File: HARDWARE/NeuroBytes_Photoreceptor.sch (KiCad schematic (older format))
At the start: 19 parts, among them P1 CONN_01X04, P2 CONN_01X04, P3 CONN_01X07, SW1 SW_PUSH, SW2 SW_PUSH, U1 APDS9007, U2 STM32L011Gx, U3 LD3985M33R

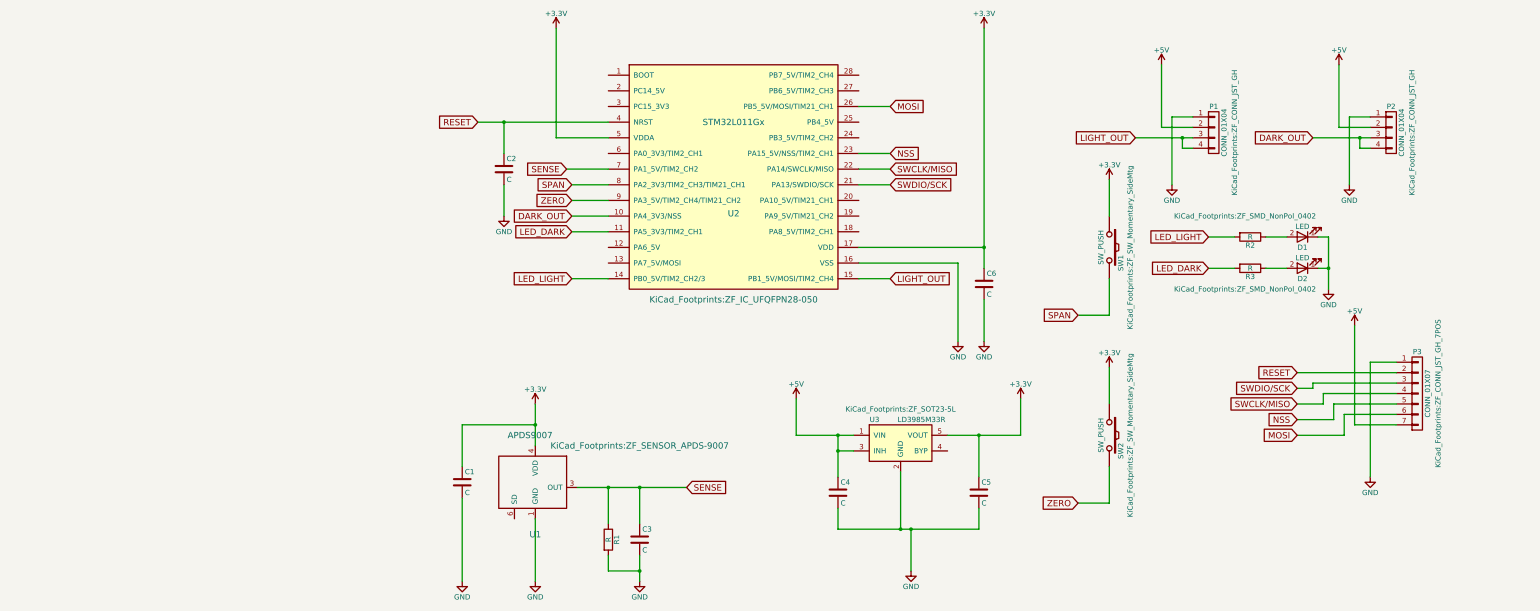
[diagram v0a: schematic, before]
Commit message: Iterated hardware design to incorporate several new features: (1) PCB outline no longer in line with cell wall; rather, entire photoreceptor is displayed on front in copper, and PCB outline is designed to nest with others. (2) Front mounted tiny pushbuttons used in place of side mounted versions for zero/span. (3) Updated title. (4) Minor modifications to footprints (such as sensor, which is now vertical).
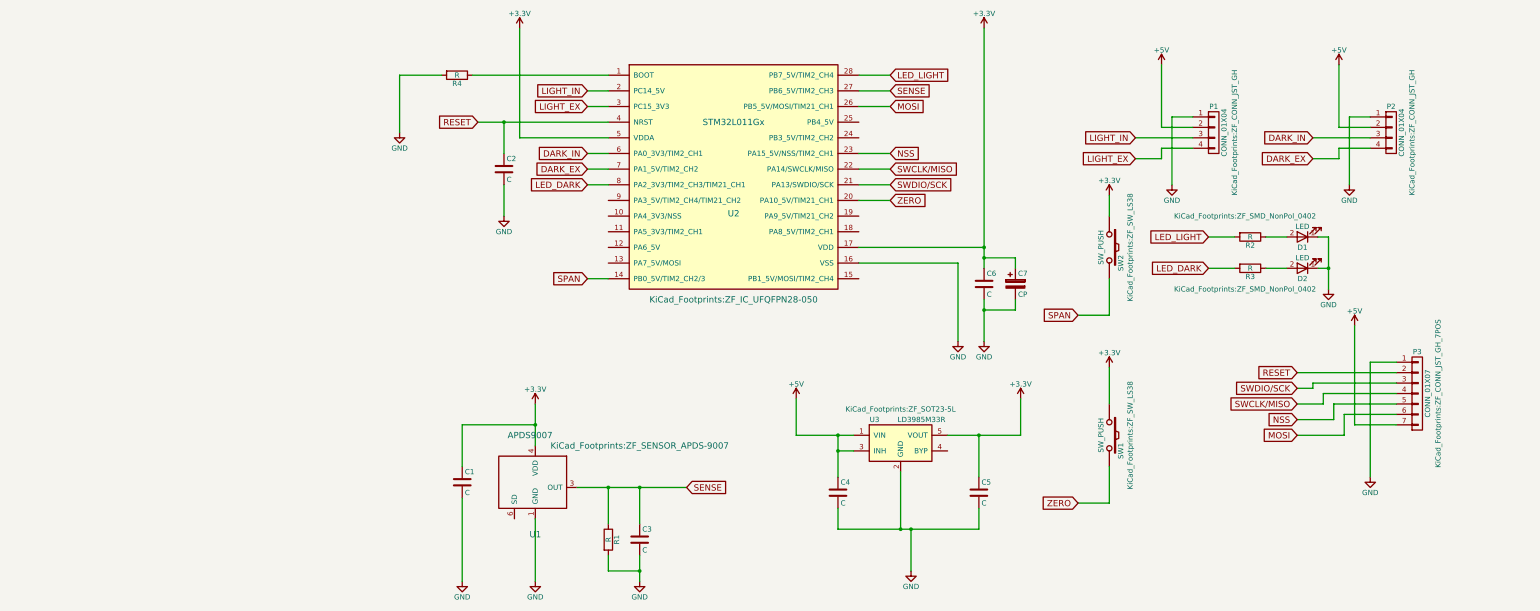
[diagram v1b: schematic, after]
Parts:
- added C7: CP, KiCad_Footprints:ZF_SMD_pol_1206, symbol CP
- added R4: R, KiCad_Footprints:ZF_SMD_NonPol_0402, symbol R
- SW1, SW2: footprint KiCad_Footprints:ZF_SW_Momentary_SideMtg -> KiCad_Footprints:ZF_SW_LS38
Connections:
- net +3V3: now also C7.1
- net GND: now also C7.2, R4.2
- net LED_DARK: now also U2.8 (PA2_3V3/TIM2_CH3/TIM21_CH1); no longer U2.11 (PA5_3V3/TIM2_CH1)
- net LED_LIGHT: now also U2.28 (PB7_5V/TIM2_CH4); no longer U2.14 (PB0_5V/TIM2_CH2/3)
- net SENSE: now also U2.27 (PB6_5V/TIM2_CH3); no longer U2.7 (PA1_5V/TIM2_CH2)
- net SPAN: now also SW2.2, U2.14 (PB0_5V/TIM2_CH2/3); no longer SW1.2, U2.8 (PA2_3V3/TIM2_CH3/TIM21_CH1)
- net ZERO: now also SW1.2, U2.20 (PA10_5V/TIM21_CH1); no longer SW2.2, U2.9 (PA3_5V/TIM2_CH4/TIM21_CH2)
- net at U2.1 (BOOT): now also R4.1
- net LIGHT_IN: now reaches U2.2 (PC14_5V)
- net LIGHT_IN: now also P1.3 (P3)
- net LIGHT_EX: now reaches U2.3 (PC15_3V3)
- net LIGHT_EX: now also P1.4 (P4)
- net DARK_IN: now reaches U2.6 (PA0_3V3/TIM2_CH1)
- net DARK_IN: now also P2.3 (P3)
- removed net DARK_OUT: P2.3 (P3), P2.4 (P4), U2.10 (PA4_3V3/NSS)
- removed net LIGHT_OUT: P1.3 (P3), P1.4 (P4), U2.15 (PB1_5V/MOSI/TIM2_CH4)
- new net DARK_EX: P2.4 (P4), U2.7 (PA1_5V/TIM2_CH2)
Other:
- moved on the sheet: SW1, SW2

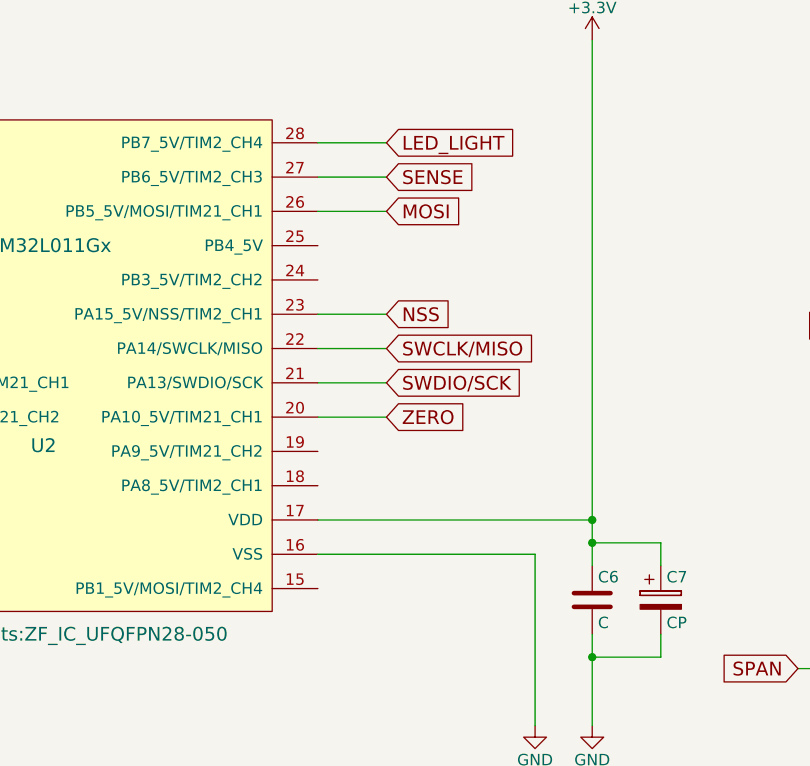
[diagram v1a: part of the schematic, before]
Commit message: Moved SENSE line from PB6 to PB1 so it's now on an ADC line (ADC9). Bodging prototypes.
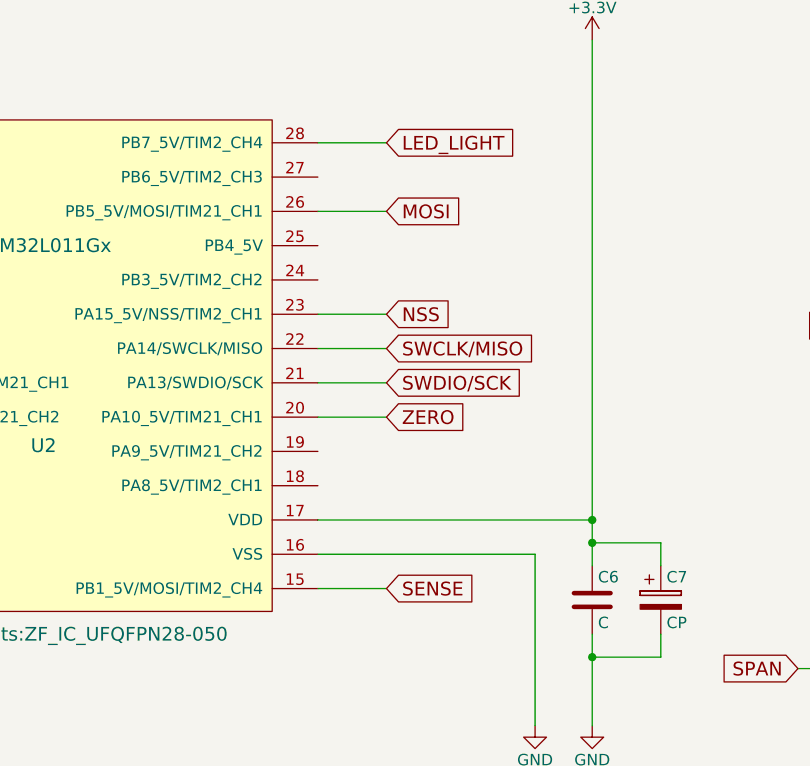
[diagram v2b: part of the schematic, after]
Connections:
- net SENSE: now also U2.15 (PB1_5V/MOSI/TIM2_CH4); no longer U2.27 (PB6_5V/TIM2_CH3)
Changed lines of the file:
@@
 Wire Wire Line
 	2900 6050 2900 5700
-Text GLabel 5600 1900 2    60   Input ~ 0
+Text GLabel 5600 3700 2    60   Input ~ 0
 SENSE
 Wire Wire Line
@@
 	2700 2650 2900 2650
 Wire Wire Line
-	5600 1900 5300 1900
-Wire Wire Line
 	5600 1750 5300 1750
 Wire Wire Line
@@
 	6800 3500 6500 3500
 Connection ~ 6500 3500
+Wire Wire Line
+	5600 3700 5300 3700
 $EndSCHEMATC

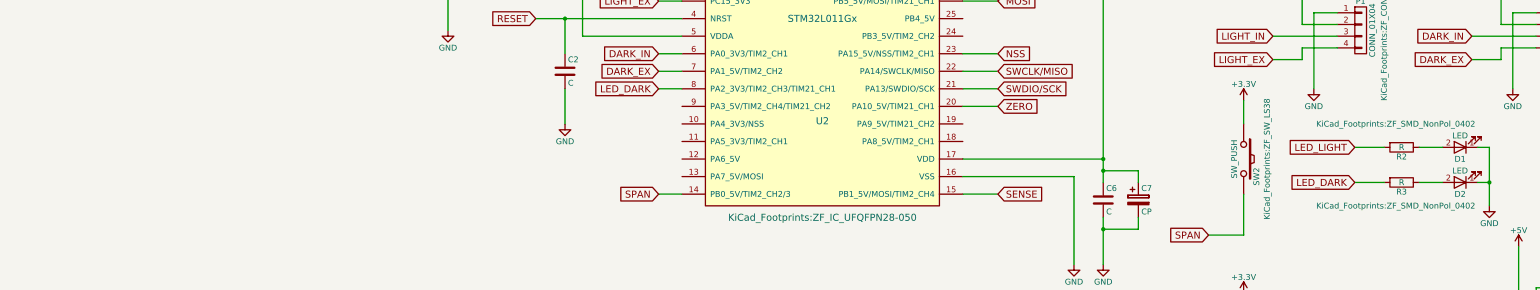
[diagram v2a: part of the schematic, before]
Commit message: Updated KiCad project file to reference library submodule
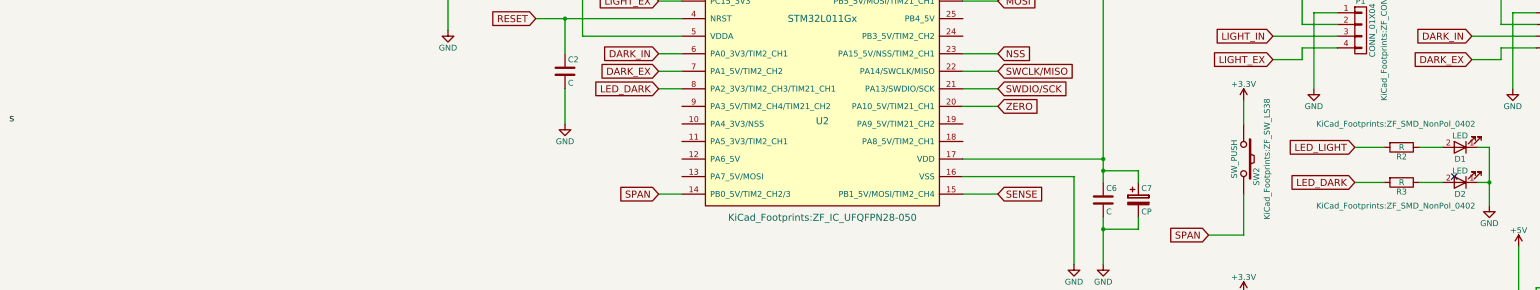
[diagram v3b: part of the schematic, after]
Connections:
- no-connect marks 0 -> 1
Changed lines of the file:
@@
 Wire Wire Line
 	5600 3700 5300 3700
+NoConn ~ 9500 3550
+Text Label -2850 3100 0    60   ~ 0
+s
 $EndSCHEMATC
